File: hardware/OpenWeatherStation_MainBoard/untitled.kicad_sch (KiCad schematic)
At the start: 50 parts, among them J1 RJ45_LED_Shielded, Q1 Q_NMOS_GDS, U5 PM8800A, U6 POE13P-33L

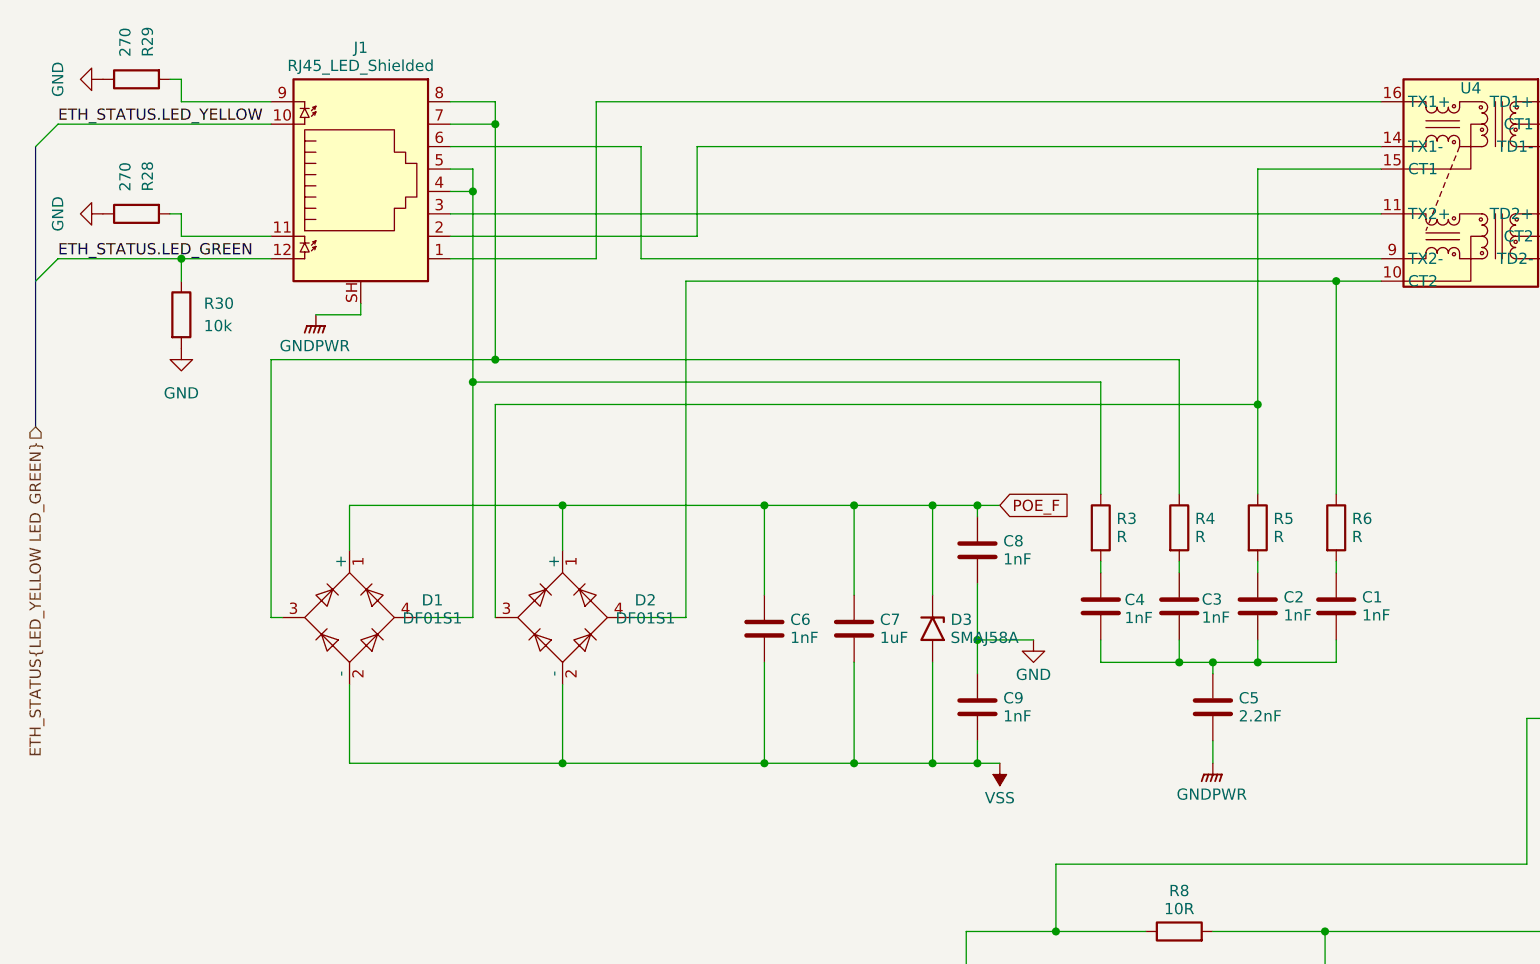
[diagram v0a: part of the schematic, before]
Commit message: move eth connector to dedicated sheet
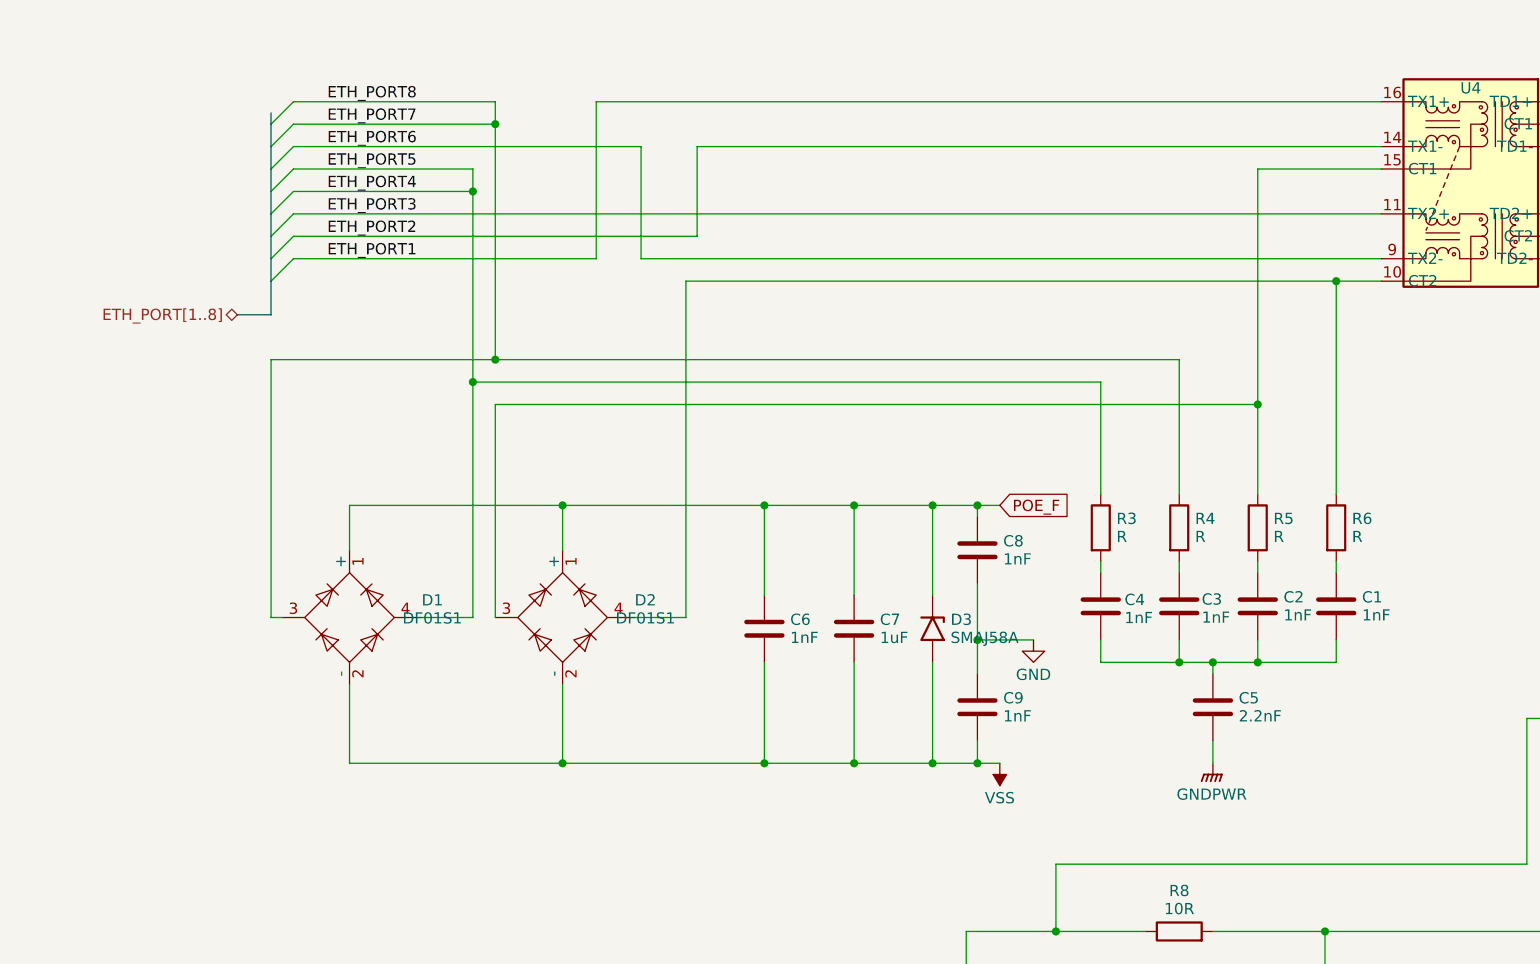
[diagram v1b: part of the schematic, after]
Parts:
- removed J1: RJ45_LED_Shielded, symbol Connector:RJ45_LED_Shielded
- removed R28, R29: 270, symbol Device:R
- removed R30: 10k, symbol Device:R
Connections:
- net ETH_PORT7: now reaches D1.3, R4.1
- net ETH_PORT4: now reaches D1.4, R3.1
- net ETH_PORT3: now reaches U4.11 (TX2+)
- net ETH_PORT2: now reaches U4.14 (TX1-)
- net ETH_PORT1: now reaches U4.16 (TX1+)
- net ETH_PORT6: now reaches U4.9 (TX2-)

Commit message: poe wip
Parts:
- R3, R4, R5, R6: value R -> 75
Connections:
- net ETH_PORT4: now also R4.1; no longer R3.1
- net ETH_PORT7: now also R3.1; no longer R4.1
- net GND: now also U6.4; no longer U6.1
- net at C13.1, L1.2, R8.1: now also U6.2; no longer U6.3
- net at Q1.2 (D): now also U6.1; no longer U6.4
- net at R17.2: now also U6.3; no longer U6.2
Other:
- moved on the sheet: C1, C2, C3, C4, C5, C8, C9, D2, R3, R4, R5, R6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

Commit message: poe wip
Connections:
- net GND: no longer C10.2, C11.2, C12.2, C13.2
- net POE_F: no longer C12.1
- net VSS: now also C10.2, C11.2, C12.2, C13.2
- net at C13.1, L1.2, R8.1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: now also C12.1
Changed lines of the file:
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@@
+    (stroke (width 0) (type default))
+  )
+  (wire (pts (xy 57.15 153.67) (xy 67.31 153.67))
     (stroke (width 0) (type default))
   )
@@
     (stroke (width 0) (type default))
   )
-  (wire (pts (xy 43.18 153.67) (xy 67.31 153.67))
+  (wire (pts (xy 43.18 153.67) (xy 49.53 153.67))
     (stroke (width 0) (type default))
   )
@@
     (stroke (width 0) (type default))
   )
-  (wire (pts (xy 67.31 153.67) (xy 71.12 153.67))
-    (stroke (width 0) (type default))
-  )
   (wire (pts (xy 63.5 48.26) (xy 63.5 45.72))
     (stroke (width 0) (type default))
@@
     (stroke (width 0) (type default))
   )
-  (wire (pts (xy 78.74 153.67) (xy 82.55 153.67))
+  (wire (pts (xy 67.31 153.67) (xy 82.55 153.67))
     (stroke (width 0) (type default))
   )
@@
     )
   )
+  (symbol (lib_id "power:VSS") (at 25.4 181.61 180) (unit 1)
+    (in_bom yes) (on_board yes) (dnp no) (fields_autoplaced)
+    (property "Reference" "#PWR01" (at 25.4 177.8 0)
+      (effects (font (size 1.27 1.27)) hide)
+    )
+    (property "Value" "VSS" (at 25.4 186.69 0)
+      (effects (font (size 1.27 1.27)))
+    )
+    (property "Footprint" "" (at 25.4 181.61 0)
+      (effects (font (size 1.27 1.27)) hide)
+    )
+    (property "Datasheet" "" (at 25.4 181.61 0)
+      (effects (font (size 1.27 1.27)) hide)
+    )
+    (pin "1")
+    (instances
+      (project "OpenWeatherStation_MainBoard"
+        (path "/698c4dde-56a2-4dd1-89d2-180a09a5dfe9/7c03bbc1-3816-4af6-9da6-b1bc735a9c60"
+          (reference "#PWR01") (unit 1)
+        )
+      )
+    )
+  )
+  (symbol (lib_id "Device:L") (at 53.34 153.67 90) (unit 1)
+    (in_bom yes) (on_board yes) (dnp no) (fields_autoplaced)
+    (property "Reference" "L1" (at 53.34 149.5847 90)
+      (effects (font (size 1.27 1.27)))
+    )
+    (property "Value" "L" (at 53.34 151.6327 90)
+      (effects (font (size 1.27 1.27)))
+    )
+    (property "Footprint" "" (at 53.34 153.67 0)
+      (effects (font (size 1.27 1.27)) hide)
+    )
+    (property "Datasheet" "~" (at 53.34 153.67 0)
+      (effects (font (size 1.27 1.27)) hide)
+    )
+    (pin "1")
+    (pin "2")
+    (instances
+      (project "OpenWeatherStation_MainBoard"
+        (path "/698c4dde-56a2-4dd1-89d2-180a09a5dfe9/7c03bbc1-3816-4af6-9da6-b1bc735a9c60"
+          (reference "L1") (unit 1)
+        )
+      )
+    )
+  )
   (symbol (lib_id "power:GND") (at 245.11 83.82 0) (unit 1)
     (in_bom yes) (on_board yes) (dnp no) (fields_autoplaced)
@@
         (path "/698c4dde-56a2-4dd1-89d2-180a09a5dfe9/7c03bbc1-3816-4af6-9da6-b1bc735a9c60"
           (reference "Q1") (unit 1)
-        )
-      )
-    )
-  )
-  (symbol (lib_id "Device:L") (at 74.93 153.67 90) (unit 1)
-    (in_bom yes) (on_board yes) (dnp no) (fields_autoplaced)
-    (property "Reference" "L1" (at 74.93 149.5847 90)
-      (effects (font (size 1.27 1.27)))
-    )
-    (property "Value" "L" (at 74.93 151.6327 90)
-      (effects (font (size 1.27 1.27)))
-    )
-    (property "Footprint" "" (at 74.93 153.67 0)
-      (effects (font (size 1.27 1.27)) hide)
-    )
-    (property "Datasheet" "~" (at 74.93 153.67 0)
-      (effects (font (size 1.27 1.27)) hide)
-    )
-    (pin "1")
-    (pin "2")
-    (instances
-      (project "OpenWeatherStation_MainBoard"
-        (path "/698c4dde-56a2-4dd1-89d2-180a09a5dfe9/7c03bbc1-3816-4af6-9da6-b1bc735a9c60"
-          (reference "L1") (unit 1)
         )
       )
@@
         )
       )
-    )
-  )
-  (symbol (lib_id "power:GND") (at 25.4 181.61 0) (unit 1)
-    (in_bom yes) (on_board yes) (dnp no) (fields_autoplaced)
-    (property "Reference" "#PWR012" (at 25.4 187.96 0)
-      (effects (font (size 1.27 1.27)) hide)
-    )
-    (property "Value" "GND" (at 25.4 185.555 0)
-      (effects (font (size 1.27 1.27)))
-    )
-    (property "Footprint" "" (at 25.4 181.61 0)
-      (effects (font (size 1.27 1.27)) hide)
-    )
-    (property "Datasheet" "" (at 25.4 181.61 0)
-      (effects (font (size 1.27 1.27)) hide)
-    )
-    (pin "1")
-    (instances
-      (project "OpenWeatherStation_MainBoard"
-        (path "/698c4dde-56a2-4dd1-89d2-180a09a5dfe9/7c03bbc1-3816-4af6-9da6-b1bc735a9c60"
-          (reference "#PWR012") (unit 1)
-        )
-      )

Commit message: update schematics
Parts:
- added NT1, NT2, NT3, NT4: NetTie_2, NetTie:NetTie-2_SMD_Pad0.5mm, symbol Device:NetTie_2
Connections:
- net ETH_PORT4: now also NT1.1; no longer D1.4, R4.1
- net ETH_PORT7: now also NT3.1; no longer D1.3, R3.1
- new net: D1.4, NT1.2, NT2.2, R4.1
- new net: D1.3, NT3.2, NT4.2, R3.1
- new net ETH_PORT5: NT2.1
- new net ETH_PORT8: NT4.1
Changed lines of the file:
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@@
   (junction (at 43.18 153.67) (diameter 0) (color 0 0 0 0)
   )
-  (junction (at 55.88 54.61) (diameter 0) (color 0 0 0 0)
-  )
   (junction (at 227.33 152.4) (diameter 0) (color 0 0 0 0)
   )
@@
   (junction (at 146.05 115.57) (diameter 0) (color 0 0 0 0)
   )
+  (junction (at 60.96 54.61) (diameter 0) (color 0 0 0 0)
+  )
   (junction (at 185.42 152.4) (diameter 0) (color 0 0 0 0)
   )
@@
     (stroke (width 0) (type default))
   )
-  (wire (pts (xy 55.88 54.61) (xy 55.88 52.07))
+  (wire (pts (xy 60.96 54.61) (xy 60.96 52.07))
     (stroke (width 0) (type default))
   )
@@
     (stroke (width 0) (type default))
   )
+  (wire (pts (xy 59.69 54.61) (xy 60.96 54.61))
+    (stroke (width 0) (type default))
+  )
   (wire (pts (xy 262.89 148.59) (xy 262.89 152.4))
     (stroke (width 0) (type default))
@@
     (stroke (width 0) (type default))
   )
+  (wire (pts (xy 38.1 54.61) (xy 54.61 54.61))
+    (stroke (width 0) (type default))
+  )
   (wire (pts (xy 195.58 30.48) (xy 195.58 36.83))
     (stroke (width 0) (type default))
@@
     (stroke (width 0) (type default))
   )
-  (wire (pts (xy 38.1 45.72) (xy 63.5 45.72))
+  (wire (pts (xy 38.1 45.72) (xy 54.61 45.72))
     (stroke (width 0) (type default))
   )
@@
     (stroke (width 0) (type default))
   )
-  (wire (pts (xy 38.1 54.61) (xy 55.88 54.61))
-    (stroke (width 0) (type default))
-  )
   (wire (pts (xy 218.44 135.89) (xy 232.41 135.89))
     (stroke (width 0) (type default))
@@
     (stroke (width 0) (type default))
   )
+  (wire (pts (xy 59.69 45.72) (xy 63.5 45.72))
+    (stroke (width 0) (type default))
+  )
   (bus (pts (xy 35.56 54.61) (xy 35.56 57.15))
     (stroke (width 0) (type default))
@@
     (stroke (width 0) (type default))
   )
+  (wire (pts (xy 59.69 52.07) (xy 60.96 52.07))
+    (stroke (width 0) (type default))
+  )
   (wire (pts (xy 262.89 152.4) (xy 252.73 152.4))
     (stroke (width 0) (type default))
@@
     (stroke (width 0) (type default))
   )
-  (wire (pts (xy 38.1 48.26) (xy 63.5 48.26))
+  (wire (pts (xy 38.1 48.26) (xy 54.61 48.26))
     (stroke (width 0) (type default))
   )
@@
     (stroke (width 0) (type default))
   )
-  (wire (pts (xy 38.1 52.07) (xy 55.88 52.07))
+  (wire (pts (xy 38.1 52.07) (xy 54.61 52.07))
     (stroke (width 0) (type default))
   )
@@
     (stroke (width 0) (type default))
   )
+  (wire (pts (xy 59.69 48.26) (xy 63.5 48.26))
+    (stroke (width 0) (type default))
+  )
   (wire (pts (xy 262.89 71.12) (xy 262.89 91.44))
     (stroke (width 0) (type default))
@@
     (stroke (width 0) (type default))
   )
-  (wire (pts (xy 55.88 58.42) (xy 43.18 58.42))
+  (wire (pts (xy 60.96 58.42) (xy 43.18 58.42))
     (stroke (width 0) (type default))
   )
@@
     (stroke (width 0) (type default))
   )
-  (wire (pts (xy 55.88 54.61) (xy 55.88 58.42))
+  (wire (pts (xy 60.96 54.61) (xy 60.96 58.42))
     (stroke (width 0) (type default))
   )
@@
     )
   )
+  (symbol (lib_id "Device:NetTie_2") (at 57.15 48.26 0) (unit 1)
+    (in_bom no) (on_board yes) (dnp no)
+    (property "Reference" "NT2" (at 57.15 49.53 0)
+      (effects (font (size 1.27 1.27)))
+    )
+    (property "Value" "NetTie_2" (at 57.15 45.72 0)
+      (effects (font (size 1.27 1.27)) hide)
+    )
+    (property "Footprint" "NetTie:NetTie-2_SMD_Pad0.5mm" (at 57.15 48.26 0)
+      (effects (font (size 1.27 1.27)) hide)
+    )
+    (property "Datasheet" "~" (at 57.15 48.26 0)
+      (effects (font (size 1.27 1.27)) hide)
+    )
+    (pin "1")
+    (pin "2")
+    (instances
+      (project "OpenWeatherStation_MainBoard"
+        (path "/698c4dde-56a2-4dd1-89d2-180a09a5dfe9/7c03bbc1-3816-4af6-9da6-b1bc735a9c60"
+          (reference "NT2") (unit 1)
+        )
+      )
+    )
+  )
   (symbol (lib_id "Device:C") (at 163.83 130.81 180) (unit 1)
     (in_bom yes) (on_board yes) (dnp no) (fields_autoplaced)
@@
         (path "/698c4dde-56a2-4dd1-89d2-180a09a5dfe9/7c03bbc1-3816-4af6-9da6-b1bc735a9c60"
           (reference "D4") (unit 1)
+        )
+      )
+    )
+  )
+  (symbol (lib_id "Device:NetTie_2") (at 57.15 54.61 0) (unit 1)
+    (in_bom no) (on_board yes) (dnp no)
+    (property "Reference" "NT4" (at 57.15 55.88 0)
+      (effects (font (size 1.27 1.27)))
+    )
+    (property "Value" "NetTie_2" (at 57.15 52.07 0)
+      (effects (font (size 1.27 1.27)) hide)
+    )
+    (property "Footprint" "NetTie:NetTie-2_SMD_Pad0.5mm" (at 57.15 54.61 0)
+      (effects (font (size 1.27 1.27)) hide)
+    )
+    (property "Datasheet" "~" (at 57.15 54.61 0)
+      (effects (font (size 1.27 1.27)) hide)
+    )
+    (pin "1")
+    (pin "2")
+    (instances
+      (project "OpenWeatherStation_MainBoard"
+        (path "/698c4dde-56a2-4dd1-89d2-180a09a5dfe9/7c03bbc1-3816-4af6-9da6-b1bc735a9c60"
+          (reference "NT4") (unit 1)
         )
       )
@@
     )
   )
+  (symbol (lib_id "Device:NetTie_2") (at 57.15 45.72 0) (unit 1)
+    (in_bom no) (on_board yes) (dnp no)
+    (property "Reference" "NT1" (at 57.15 46.99 0)
+      (effects (font (size 1.27 1.27)))
+    )
+    (property "Value" "NetTie_2" (at 57.15 43.18 0)
+      (effects (font (size 1.27 1.27)) hide)
+    )
+    (property "Footprint" "NetTie:NetTie-2_SMD_Pad0.5mm" (at 57.15 45.72 0)
+      (effects (font (size 1.27 1.27)) hide)
+    )
+    (property "Datasheet" "~" (at 57.15 45.72 0)
+      (effects (font (size 1.27 1.27)) hide)
+    )
+    (pin "1")
+    (pin "2")
+    (instances
+      (project "OpenWeatherStation_MainBoard"
+        (path "/698c4dde-56a2-4dd1-89d2-180a09a5dfe9/7c03bbc1-3816-4af6-9da6-b1bc735a9c60"
+          (reference "NT1") (unit 1)
+        )
+      )
+    )
+  )
   (symbol (lib_id "Device:R") (at 177.8 142.24 0) (unit 1)
     (in_bom yes) (on_board yes) (dnp no) (fields_autoplaced)
@@
         )
       )
+    )
+  )
+  (symbol (lib_id "Device:NetTie_2") (at 57.15 52.07 0) (unit 1)
+    (in_bom no) (on_board yes) (dnp no)
+    (property "Reference" "NT3" (at 57.15 53.34 0)
+      (effects (font (size 1.27 1.27)))
+    )
+    (property "Value" "NetTie_2" (at 57.15 49.53 0)
+      (effects (font (size 1.27 1.27)) hide)
+    )
+    (property "Footprint" "NetTie:NetTie-2_SMD_Pad0.5mm" (at 57.15 52.07 0)
+      (effects (font (size 1.27 1.27)) hide)
+    )
+    (property "Datasheet" "~" (at 57.15 52.07 0)
+      (effects (font (size 1.27 1.27)) hide)
+    )
+    (pin "1")
+    (pin "2")
+    (instances
+      (project "OpenWeatherStation_MainBoard"
+        (path "/698c4dde-56a2-4dd1-89d2-180a09a5dfe9/7c03bbc1-3816-4af6-9da6-b1bc735a9c60"
+          (reference "NT3") (unit 1)
+        )
+      )

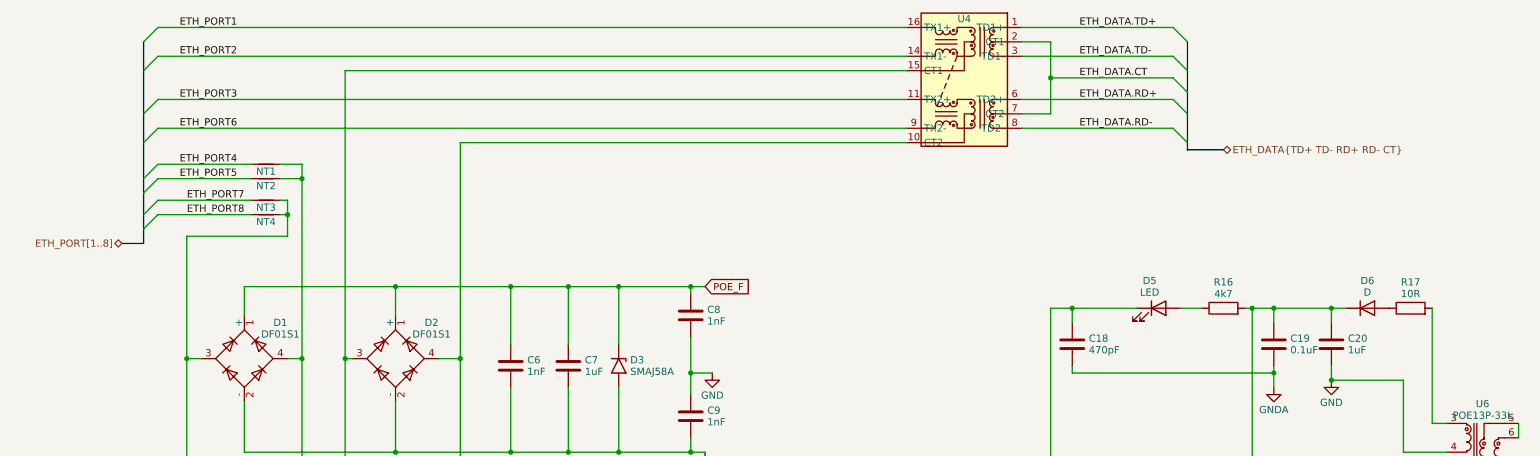
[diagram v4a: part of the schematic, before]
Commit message: schematic update
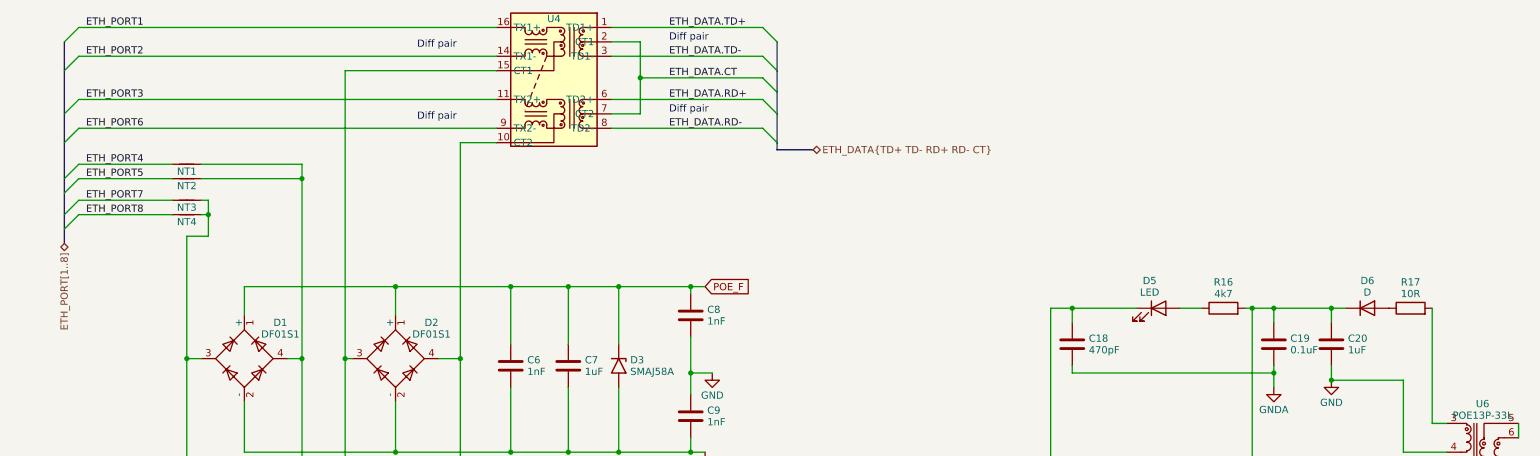
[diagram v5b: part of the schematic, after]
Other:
- note added: "Diff pair"
- moved on the sheet: NT1, NT2, NT3, NT4, U4
